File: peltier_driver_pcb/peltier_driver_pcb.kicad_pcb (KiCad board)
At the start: 2 copper layers, 5 parts, among them U1 LCD-016N002L

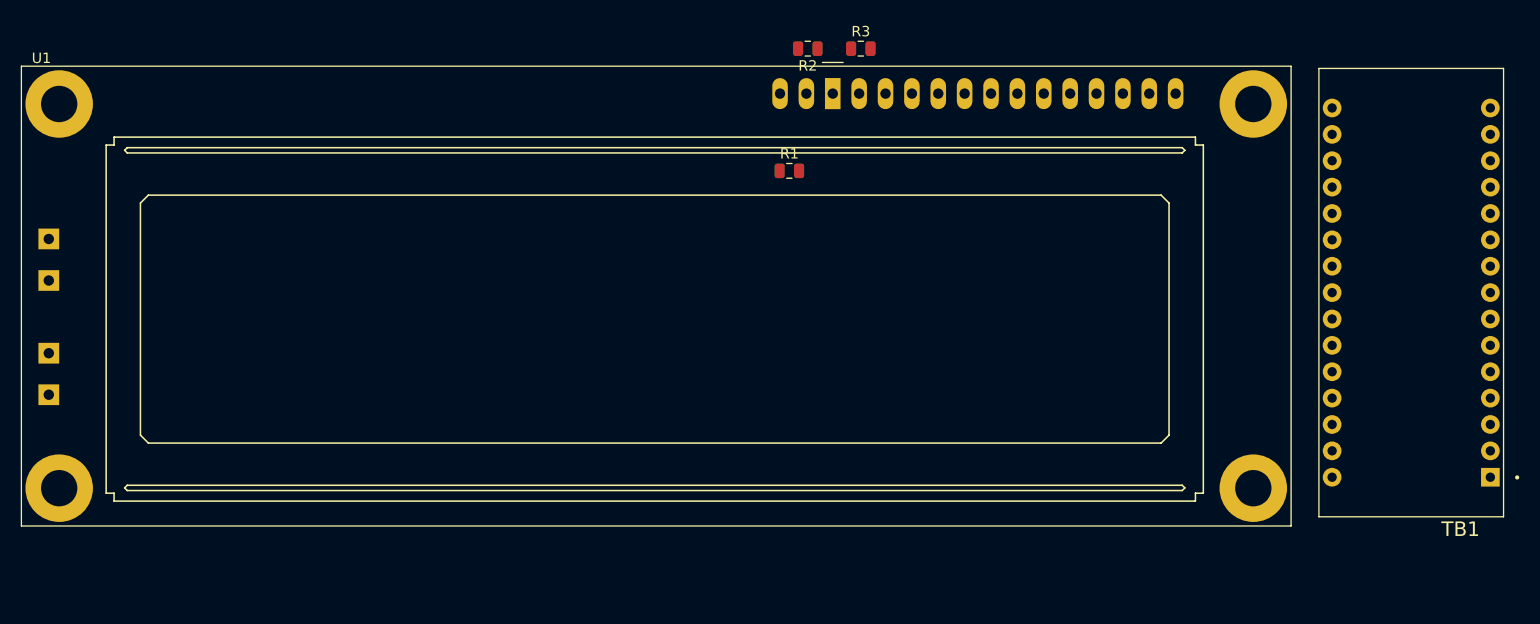
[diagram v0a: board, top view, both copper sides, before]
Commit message: added I-sense IC and 128x32 OLED footprint
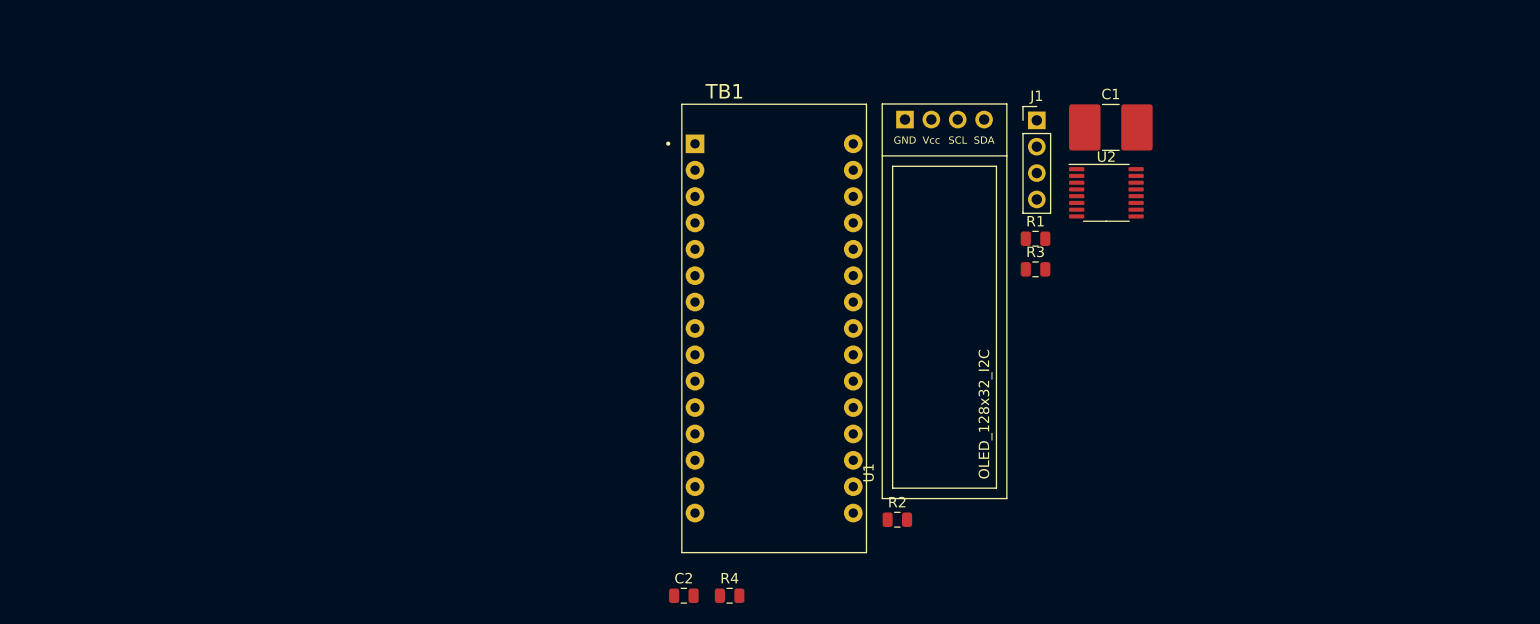
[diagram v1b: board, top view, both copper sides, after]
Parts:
- added C1: C_BUS, Capacitor_SMD:C_2816_7142Metric, F.Cu at (177.4, 34.3)
- added C2: 0.1uF, Capacitor_SMD:C_0805_2012Metric, F.Cu at (136.3, 79.4)
- added J1: Conn_01x04, Connector_PinHeader_2.54mm:PinHeader_1x04_P2.54mm_Vertical, F.Cu at (170.3, 33.6)
- added R4: 4K7, Resistor_SMD:R_0805_2012Metric, F.Cu at (140.7, 79.4)
- added U2: INA260, Package_SO:TSSOP-16_4.4x5mm_P0.65mm, F.Cu at (177.0, 40.6)
- R1: value 5K -> 4k7
- R2: value 10 -> 4k7
- R3: value 5K -> 4K7
- TB1: footprint SHIELD_ARDUINO_NANO -> ARDUINO_NANO:SHIELD_ARDUINO_NANO
- U1: value LCD-016N002L -> OLED_128x32_I2C; footprint Display:LCD-016N002L -> peltier_driver_pcb:OLED_128x32_I2C
- moved TB1 61.5 mm to (145.0, 53.6), turned to 0 degrees
- moved R2 46.2 mm to (156.9, 72.0), turned to 0 degrees
- moved R3 27.1 mm to (170.2, 47.9)
- moved R1 24.6 mm to (170.2, 45.0)
- moved U1 4.87 mm to (155.4, 32.0)
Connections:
- R1 pad 1: +5V -> +3V3
- R1 pad 2: Net-(R1-Pad2) -> SDA
- R2 pad 1: GND -> +3V3
- R2 pad 2: Net-(R2-Pad2) -> SCL
- R3 pad 1: GND -> +5V
- R3 pad 2: Net-(R1-Pad2) -> SDA
- TB1 pad 10: LCD_E -> Net-(TB1-Pad10)
- TB1 pad 11: LCD_RW -> Net-(TB1-Pad11)
- TB1 pad 12: LCD_RS -> Net-(TB1-Pad12)
- TB1 pad 13: LCD_DS4 -> Net-(TB1-Pad13)
- TB1 pad 14: LCD_DS5 -> Net-(TB1-Pad14)
- TB1 pad 15: LCD_DS6 -> Net-(TB1-Pad15)
- TB1 pad 16: LCD_DS7 -> Net-(TB1-Pad16)
- TB1 pad 7: Net-(TB1-Pad7) -> SDA
- TB1 pad 8: Net-(TB1-Pad8) -> SCL
- U1 pad 1: GND -> +3V3
- U1 pad 2: +3V3 -> SCL
- U1 pad 3: Net-(R1-Pad2) -> SDA
